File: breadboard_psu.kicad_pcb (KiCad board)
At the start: 2 copper layers, 55.2 x 71.1 mm, 21 parts, among them J1 Barrel_Jack_MountingPin, J2 Conn_01x02, J3 locked, J4 Conn_02x04_Odd_Even, J5 Conn_01x02, SW1 SW_DPDT_x2, SW2 SW_DPDT_x2, U1 LM317_TO-220

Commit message: DEL 5mm
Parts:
- D2: footprint LED_THT:LED_D3.0mm -> LED_THT:LED_D5.0mm
- moved D2 0.47 mm to (132.6, 105.9)
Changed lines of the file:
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@@
     (descr "DC Barrel Jack")
     (tags "Power Jack")
+    (property "MPN" "PJ-002A")
+    (property "SPN" "CP-002A-ND")
     (property "Sheetfile" "breadboard_psu.kicad_sch")
     (property "Sheetname" "")
@@
     (descr "TO-220-3, Horizontal, RM 2.54mm, see https://www.vishay.com/docs/66542/to-220-1.pdf")
     (tags "TO-220-3 Horizontal RM 2.54mm")
+    (property "MPN" "LM317KCS")
+    (property "SPN" "296-13869-5-ND")
     (property "Sheetfile" "breadboard_psu.kicad_sch")
     (property "Sheetname" "")
@@
     (descr "Diode, DO-41_SOD81 series, Axial, Horizontal, pin pitch=10.16mm, , length*diameter=5.2*2.7mm^2, , http://www.diodes.com/_files/packages/DO-41%20(Plastic).pdf")
     (tags "Diode DO-41_SOD81 series Axial Horizontal pin pitch 10.16mm  length 5.2mm diameter 2.7mm")
+    (property "MPN" "1N4001-T")
+    (property "SPN" "1N4001DICT-ND")
     (property "Sheetfile" "breadboard_psu.kicad_sch")
     (property "Sheetname" "")
@@
     (property "Height" "8mm")
     (property "MPN" "35ML10MEFCT54X7")
+    (property "SPN" "1189-3733-1-ND")
     (property "Sheetfile" "breadboard_psu.kicad_sch")
     (property "Sheetname" "")
@@
     (tags "C Axial series Axial Horizontal pin pitch 7.5mm  length 3.8mm diameter 2.6mm")
     (property "MPN" "K104K15X7RF5TL2")
+    (property "SPN" "BC1084CT-ND")
     (property "Sheetfile" "breadboard_psu.kicad_sch")
     (property "Sheetname" "")
@@
     )
   )
-  (footprint "LED_THT:LED_D3.0mm" (layer "F.Cu")
-    (at 132.085 105.918 180)
-    (descr "LED, diameter 3.0mm, 2 pins")
-    (tags "LED diameter 3.0mm 2 pins")
+  (footprint "LED_THT:LED_D5.0mm" (layer "F.Cu")
+    (at 132.5534 105.918 180)
+    (descr "LED, diameter 5.0mm, 2 pins, http://cdn-reichelt.de/documents/datenblatt/A500/LL-504BC2E-009.pdf")
+    (tags "LED diameter 5.0mm 2 pins")
     (property "Sheetfile" "breadboard_psu.kicad_sch")
     (property "Sheetname" "")
@@
     (property "ki_keywords" "LED diode")
     (attr through_hole)
-    (fp_text reference "D2" (at 1.27 -2.96) (layer "F.SilkS")
-        (effects (font (size 1 1) (thickness 0.15)))
-    )
-    (fp_text value "LED" (at 1.27 2.96) (layer "F.Fab")
-        (effects (font (size 1 1) (thickness 0.15)))
-    )
-    (fp_line (start -0.29 -1.236) (end -0.29 -1.08)
-      (stroke (width 0.12) (type solid)) (layer "F.SilkS"))
-    (fp_line (start -0.29 1.08) (end -0.29 1.236)
-      (stroke (width 0.12) (type solid)) (layer "F.SilkS"))
-    (fp_arc (start -0.29 -1.235516) (mid 1.366487 -1.987659) (end 2.942335 -1.078608)
-      (stroke (width 0.12) (type solid)) (layer "F.SilkS"))
-    (fp_arc (start 0.229039 -1.08) (mid 1.270117 -1.5) (end 2.31113 -1.079837)
-      (stroke (width 0.12) (type solid)) (layer "F.SilkS"))
-    (fp_arc (start 2.31113 1.079837) (mid 1.270117 1.5) (end 0.229039 1.08)
-      (stroke (width 0.12) (type solid)) (layer "F.SilkS"))
-    (fp_arc (start 2.942335 1.078608) (mid 1.366487 1.987659) (end -0.29 1.235516)
-      (stroke (width 0.12) (type solid)) (layer "F.SilkS"))
-    (fp_line (start -1.15 -2.25) (end -1.15 2.25)
-      (stroke (width 0.05) (type solid)) (layer "F.CrtYd"))
-    (fp_line (start -1.15 2.25) (end 3.7 2.25)
-      (stroke (width 0.05) (type solid)) (layer "F.CrtYd"))
-    (fp_line (start 3.7 -2.25) (end -1.15 -2.25)
-      (stroke (width 0.05) (type solid)) (layer "F.CrtYd"))
-    (fp_line (start 3.7 2.25) (end 3.7 -2.25)
-      (stroke (width 0.05) (type solid)) (layer "F.CrtYd"))
-    (fp_line (start -0.23 -1.16619) (end -0.23 1.16619)
-      (stroke (width 0.1) (type solid)) (layer "F.Fab"))
-    (fp_arc (start -0.23 -1.16619) (mid 3.17 0.000452) (end -0.230555 1.165476)
-      (stroke (width 0.1) (type solid)) (layer "F.Fab"))
-    (fp_circle (center 1.27 0) (end 2.77 0)
+    (fp_text reference "D2" (at 1.27 -3.96 180) (layer "F.SilkS")
+        (effects (font (size 1 1) (thickness 0.15)))
+    )
+    (fp_text value "LED" (at 1.27 3.96 180) (layer "F.Fab")
+        (effects (font (size 1 1) (thickness 0.15)))
+    )
+    (fp_text user "${REFERENCE}" (at 1.25 0 180) (layer "F.Fab")
+        (effects (font (size 0.8 0.8) (thickness 0.2)))
+    )
+    (fp_line (start -1.29 -1.545) (end -1.29 1.545)
+      (stroke (width 0.12) (type solid)) (layer "F.SilkS"))
+    (fp_arc (start -1.29 -1.54483) (mid 2.072002 -2.880433) (end 4.26 0.000462)
+      (stroke (width 0.12) (type solid)) (layer "F.SilkS"))
+    (fp_arc (start 4.26 -0.000462) (mid 2.072002 2.880433) (end -1.29 1.54483)
+      (stroke (width 0.12) (type solid)) (layer "F.SilkS"))
+    (fp_circle (center 1.27 0) (end 3.77 0)
+      (stroke (width 0.12) (type solid)) (fill none) (layer "F.SilkS"))
+    (fp_line (start -1.95 -3.25) (end -1.95 3.25)
+      (stroke (width 0.05) (type solid)) (layer "F.CrtYd"))
+    (fp_line (start -1.95 3.25) (end 4.5 3.25)
+      (stroke (width 0.05) (type solid)) (layer "F.CrtYd"))
+    (fp_line (start 4.5 -3.25) (end -1.95 -3.25)
+      (stroke (width 0.05) (type solid)) (layer "F.CrtYd"))
+    (fp_line (start 4.5 3.25) (end 4.5 -3.25)
+      (stroke (width 0.05) (type solid)) (layer "F.CrtYd"))
+    (fp_line (start -1.23 -1.469694) (end -1.23 1.469694)
+      (stroke (width 0.1) (type solid)) (layer "F.Fab"))
+    (fp_arc (start -1.23 -1.469694) (mid 4.17 0.000016) (end -1.230016 1.469666)
+      (stroke (width 0.1) (type solid)) (layer "F.Fab"))
+    (fp_circle (center 1.27 0) (end 3.77 0)
       (stroke (width 0.1) (type solid)) (fill none) (layer "F.Fab"))
     (pad "1" thru_hole rect (at 0 0 180) (size 1.8 1.8) (drill 0.9) (layers "*.Cu" "*.Mask")
@@
     (pad "2" thru_hole circle (at 2.54 0 180) (size 1.8 1.8) (drill 0.9) (layers "*.Cu" "*.Mask")
       (net 5 "Net-(D2-A)") (pinfunction "A") (pintype "passive"))
-    (model "${KICAD6_3DMODEL_DIR}/LED_THT.3dshapes/LED_D3.0mm.wrl"
-      (offset (xyz 0 0 -2.794))
+    (model "${KICAD6_3DMODEL_DIR}/LED_THT.3dshapes/LED_D5.0mm.wrl"
+      (offset (xyz 0 0 -2.5))
       (scale (xyz 1 1 1))
       (rotate (xyz 0 0 0))
@@
     (property "Height" "12.50mm")
     (property "MPN" "ESK107M025AE3EA")
+    (property "SPN" "399-6650-1-ND")
     (property "Sheetfile" "breadboard_psu.kicad_sch")
     (property "Sheetname" "")
@@
     (pts (xy 144.78 71.12) (xy 144.78 119.126))
     (height -7.62)
-    (gr_text "1890.0000 mils" (at 150.6 95.123 90) (layer "Dwgs.User")
+    (gr_text "48,0060 mm" (at 150.6 95.123 90) (layer "Dwgs.User")
       (effects (font (size 1.5 1.5) (thickness 0.3)))
     )
@@
     (pts (xy 95.885 63.5) (xy 132.334 63.5))
     (height -8.382)
-    (gr_text "1435.0000 mils" (at 114.1095 53.318) (layer "Dwgs.User")
+    (gr_text "36,4490 mm" (at 114.1095 53.318) (layer "Dwgs.User")
       (effects (font (size 1.5 1.5) (thickness 0.3)))
     )
@@
   (arc (start 110.744 69.85) (mid 111.307962 70.694029) (end 111.506 71.68963) (width 1.016) (layer "F.Cu") (net 4))
   (arc (start 110.49 69.23679) (mid 110.556012 69.568657) (end 110.744 69.85) (width 1.016) (layer "F.Cu") (net 4))
-  (segment (start 125.984 105.918) (end 129.545 105.918) (width 1.016) (layer "F.Cu") (net 5))
+  (segment (start 125.984 105.918) (end 130.0134 105.918) (width 1) (layer "F.Cu") (net 5))
   (segment (start 117.28263 85.471) (end 121.254185 85.471) (width 1.016) (layer "F.Cu") (net 6))
   (segment (start 114.722 89.154) (end 114.722 87.973647) (width 1.016) (layer "F.Cu") (net 6))

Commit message: 4 pin par tab
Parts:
- J2: value Conn_01x02 -> Conn_02x02_Odd_Even; footprint Connector_PinHeader_2.54mm:PinHeader_1x02_P2.54mm_Vertical -> Connector_PinHeader_2.54mm:PinHeader_2x02_P2.54mm_Vertical
- J3: value locked -> Conn_02x02_Odd_Even; footprint Connector_PinHeader_2.54mm:PinHeader_1x02_P2.54mm_Vertical -> Connector_PinHeader_2.54mm:PinHeader_2x02_P2.54mm_Vertical
- moved J2 2.80 mm to (144.7, 70.9), turned to 180 degrees
- moved J3 0.10 mm to (144.7, 116.6)
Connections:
- J2 pad 2: GND -> VCC
- J3 pad 2: GND -> VCC

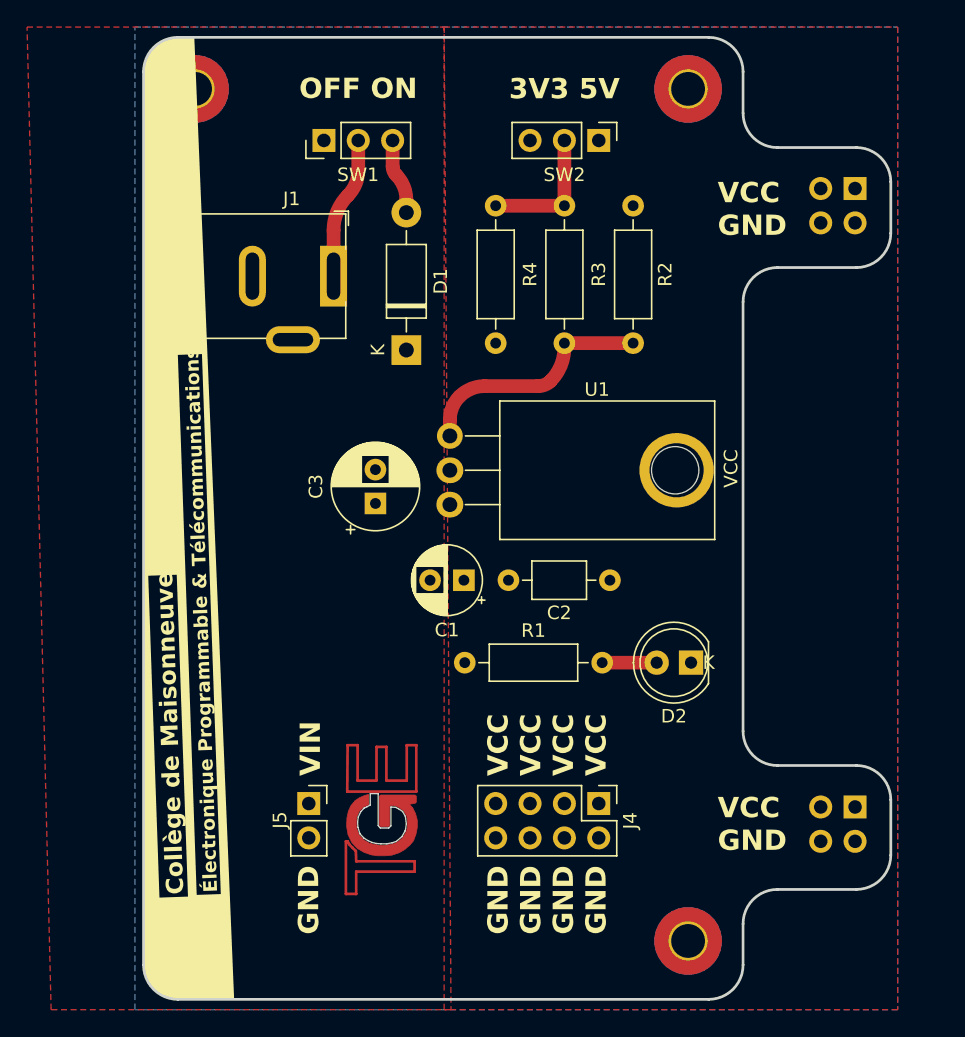
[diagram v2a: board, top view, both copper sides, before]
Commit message: Largeur des tab fixé. Nouveau contour de carte
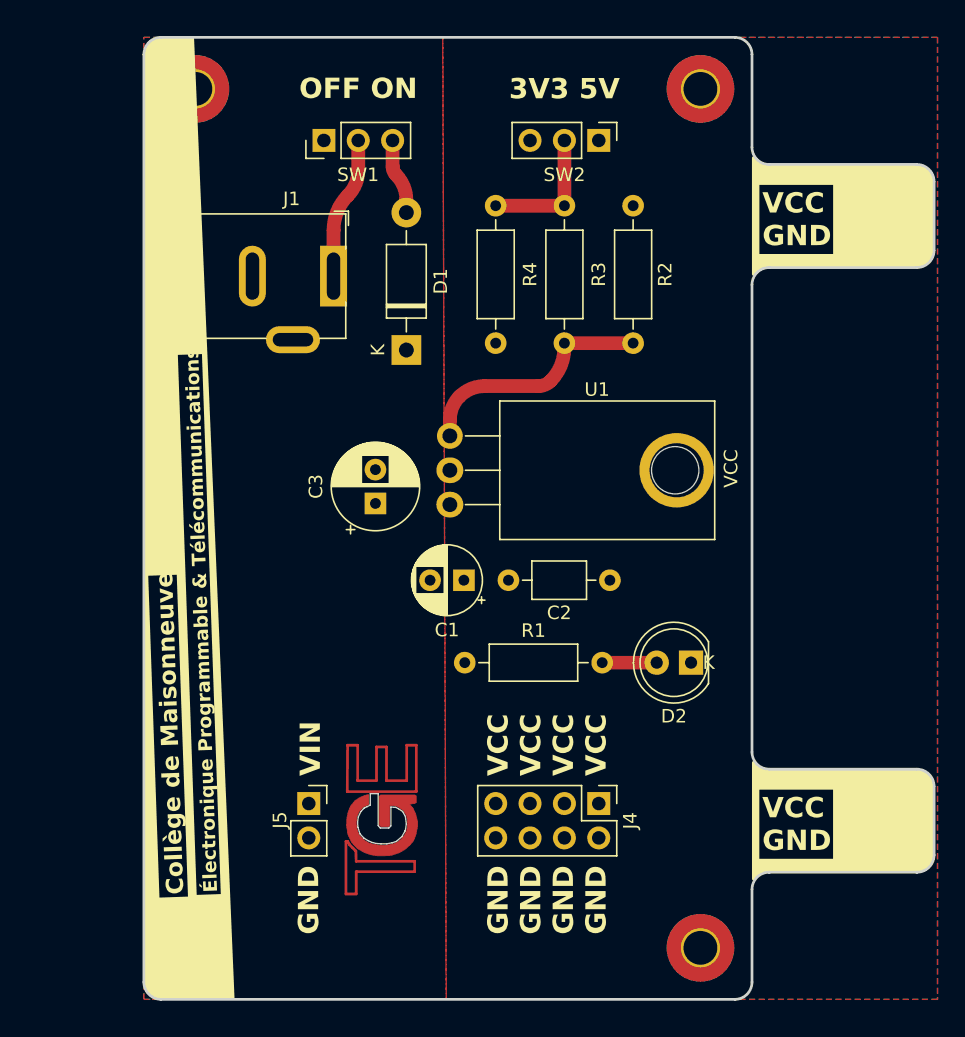
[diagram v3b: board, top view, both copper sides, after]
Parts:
- moved J2 3.39 mm to (148.0, 71.6)
- moved J3 3.31 mm to (148.0, 116.3)
- moved H4 1.05 mm to (133.2, 127.0)
- moved H3 0.91 mm to (133.2, 63.5)
- moved H2 0.51 mm to (95.9, 127.0)
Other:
- board size 55.2 x 71.1 mm -> 58.4 x 71.1 mm

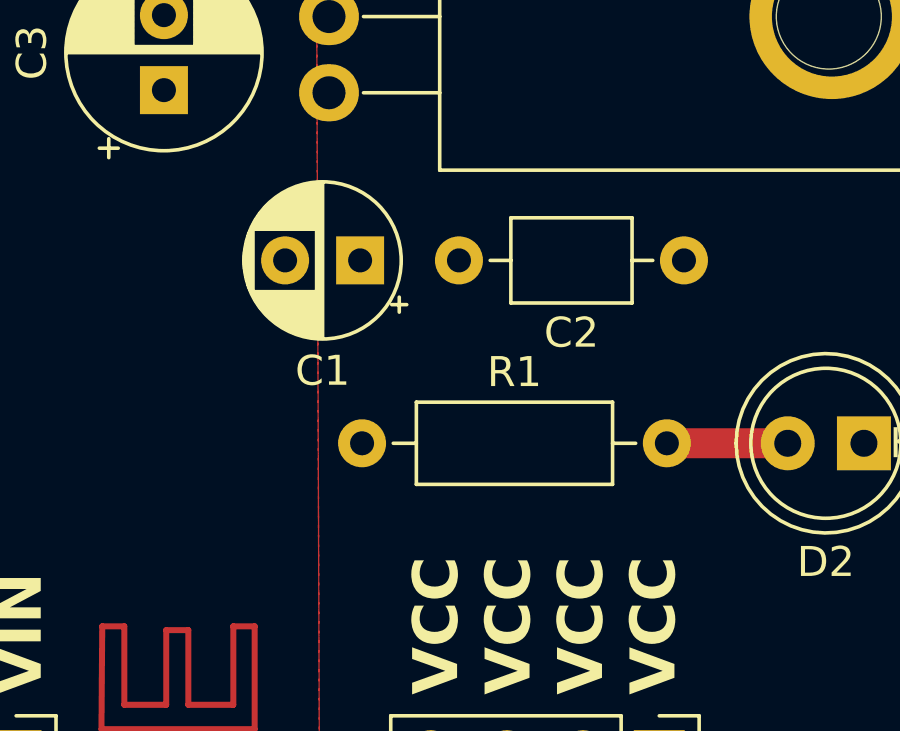
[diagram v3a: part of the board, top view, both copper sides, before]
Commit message: Info des composants a jour
MPN SPN footprint 3D
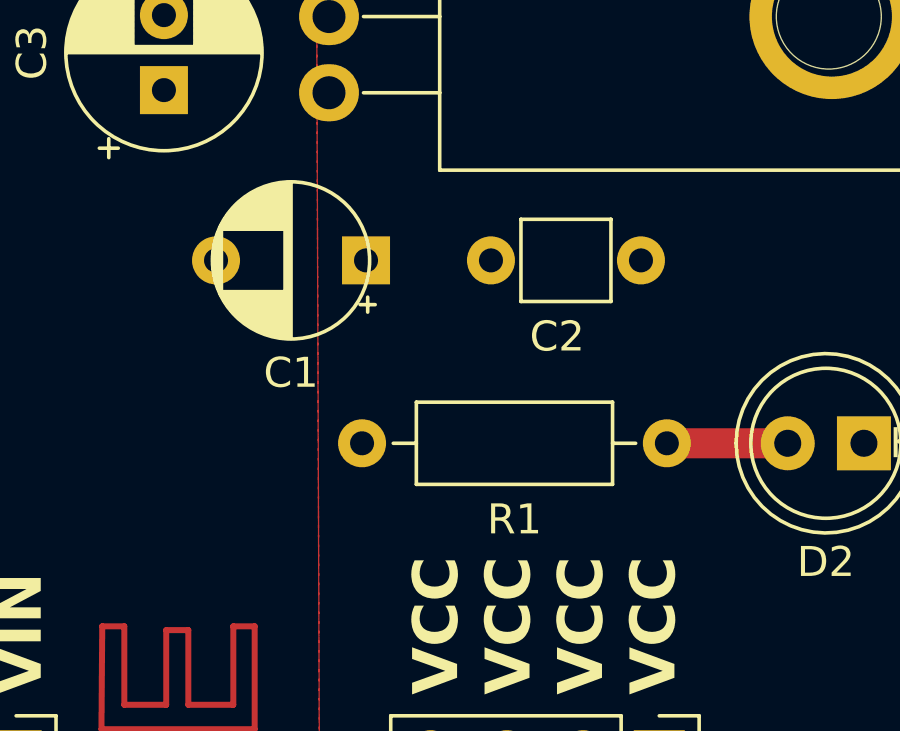
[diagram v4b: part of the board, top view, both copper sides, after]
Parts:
- C1: footprint Capacitor_THT:CP_Radial_D5.0mm_P2.50mm -> Library:CP_Radial_D5.0mm_P5.0mm_EEU-EB1J100SB
- C2: footprint Capacitor_THT:C_Axial_L3.8mm_D2.6mm_P7.50mm_Horizontal -> Library:C_Rect_L4.0mm_W2.5mm_P5.00mm_RDER71H104K0K1H03B
- moved C2 1.07 mm to (120.1, 99.8)
- moved C1 1.05 mm to (114.7, 99.8)

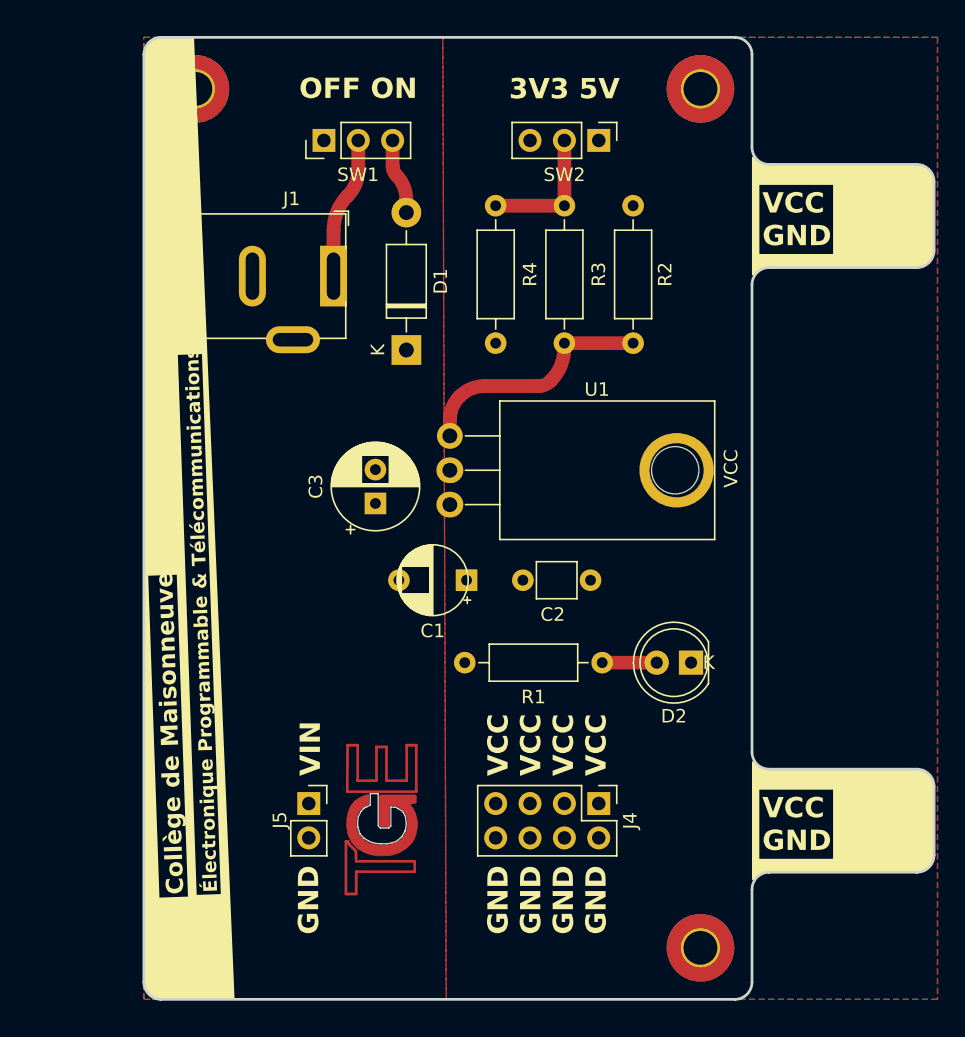
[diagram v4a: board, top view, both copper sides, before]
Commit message: Changement du silkscreen + Resistance & diode 300mils
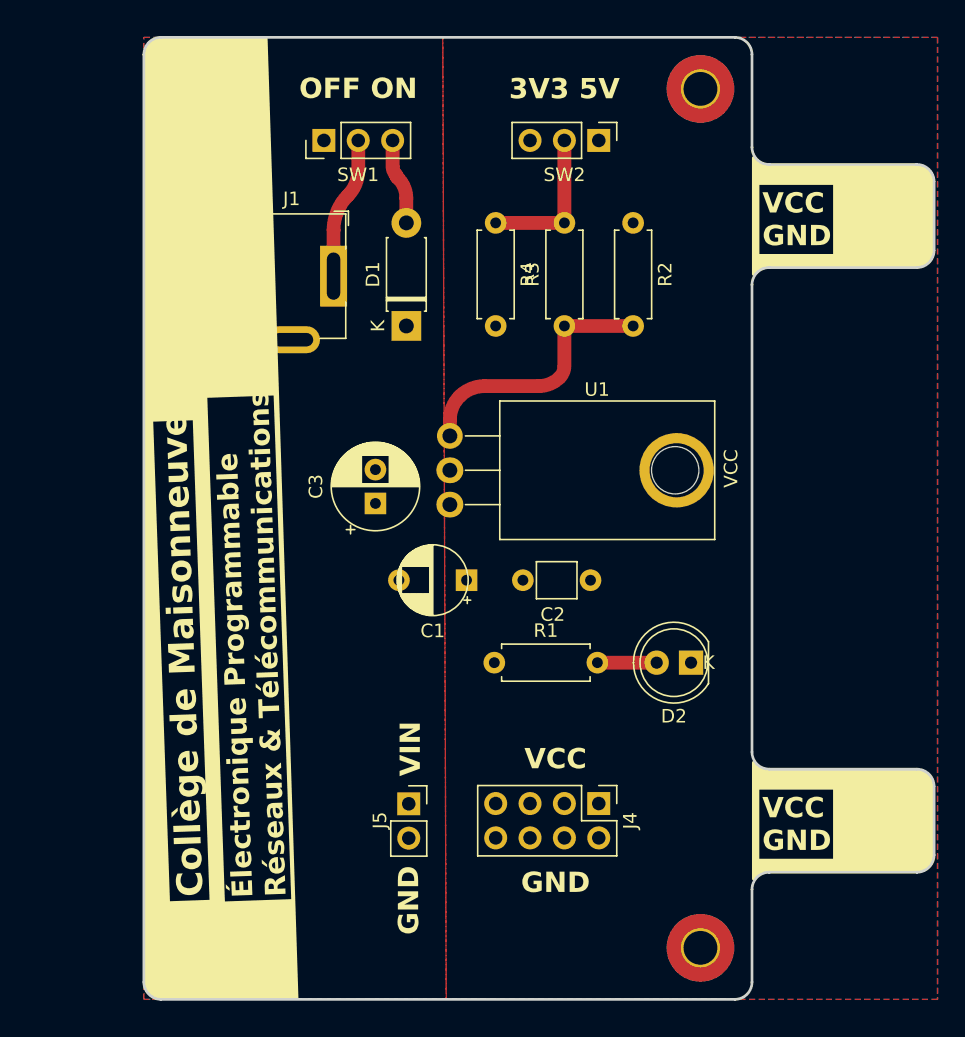
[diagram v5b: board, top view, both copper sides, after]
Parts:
- D1: footprint Diode_THT:D_DO-41_SOD81_P10.16mm_Horizontal -> Diode_THT:D_DO-41_SOD81_P7.62mm_Horizontal
- R1, R2, R3, R4: footprint Resistor_THT:R_Axial_DIN0207_L6.3mm_D2.5mm_P10.16mm_Horizontal -> Resistor_THT:R_Axial_DIN0207_L6.3mm_D2.5mm_P7.62mm_Horizontal
- moved J5 7.39 mm to (111.7, 116.4)
- moved R1 2.18 mm to (118.0, 105.9)
- moved D1 1.78 mm to (111.5, 81.0)
- moved R2 1.27 mm to (128.3, 73.4)
- moved R3 1.27 mm to (123.2, 81.0)
- moved R4 1.27 mm to (118.1, 73.4)
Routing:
- net Net-(U1-ADJ): track 18.2 -> 19.8 mm
- net Net-(SW2A-B): track 9.91 -> 11.2 mm
- net Net-(D1-A): track 5.59 -> 6.36 mm
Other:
- outline, holes or cut-outs redrawn
- board text added: "Électronique Programmable Réseaux & Télécommunications"
- board text removed: "GND GND GND GND"
- board text removed: "VCC VCC VCC VCC"
- board text removed: "Électronique Programmable & Télécommunications"

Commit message: Finalisation silkscreen
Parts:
- added G***: LOGO, LOGO, F.Cu at (105.8, 128.5)
- moved C3 4.06 mm to (109.2, 90.1)
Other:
- board text added: "9V-37V DC 1.5A max."
- board text added: "Carte d'alimentation de prototypage"
- board text added: "PCB rev. 1"
- board text removed: "2023"

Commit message: Trous et Beignes oversized
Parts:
- C3: footprint Capacitor_THT:CP_Radial_D6.3mm_P2.50mm -> Library:CP_Radial_D6.3mm_P2.50mm_Oversized
- D1: footprint Diode_THT:D_DO-41_SOD81_P7.62mm_Horizontal -> Library:D_DO-41_SOD81_P7.62mm_Horizontal_Oversized
- D2: footprint LED_THT:LED_D5.0mm -> Library:LED_D5.0mm_Oversized
- J1: footprint Connector_BarrelJack:BarrelJack_Horizontal_PJ-002A -> Library:BarrelJack_Horizontal_PJ-002A_Oversized
- J2, J3: footprint Connector_PinHeader_2.54mm:PinHeader_2x02_P2.54mm_Vertical -> Library:PinHeader_2x02_P2.54mm_Vertical_Oversized
- J4: footprint Connector_PinHeader_2.54mm:PinHeader_2x04_P2.54mm_Vertical -> Library:PinHeader_2x04_P2.54mm_Vertical_Oversized
- J5: footprint Connector_PinSocket_2.54mm:PinSocket_1x02_P2.54mm_Vertical -> Library:PinSocket_1x02_P2.54mm_Vertical_Oversized
- R1, R2, R3, R4: footprint Resistor_THT:R_Axial_DIN0207_L6.3mm_D2.5mm_P7.62mm_Horizontal -> Library:R_Axial_DIN0207_L6.3mm_D2.5mm_P7.62mm_Horizontal_Oversized
- SW1, SW2: footprint Connector_PinHeader_2.54mm:PinHeader_1x03_P2.54mm_Vertical -> Library:PinHeader_1x03_P2.54mm_Vertical_Oversized
- U1: footprint Package_TO_SOT_THT:TO-220-3_Horizontal_TabDown_Connected -> Library:TO-220-3_Horizontal_TabDown_Connected_Oversized
